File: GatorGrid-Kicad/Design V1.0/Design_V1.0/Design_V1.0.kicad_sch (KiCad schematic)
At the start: 10 parts, among them J1 Conn_01x02, U1 TP4056

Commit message: added all the symbols
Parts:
- added C1, C2: 100nF, symbol Device:C
- added F1: Polyfuse, symbol Device:Polyfuse
- added SW1: SW_SPST, symbol Switch:SW_SPST
- A1: value RaspberryPi_Pico -> RPICO-AP
- A2: value RaspberryPi_Pico -> RPICO-STA
- J1: value Conn_01x02 -> Battery-Connector
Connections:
- net GND: now also C1.2, C2.2
- net VBAT(+): now also SW1.2 (B); no longer D1.2 (A)
- net VSYS: now also C1.1, C2.1
- new net: F1.2, SW1.1 (A)
- new net: D1.2 (A), F1.1
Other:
- moved on the sheet: A1, A2, D1, D2, D3, J1, R1, R2, R3, U1

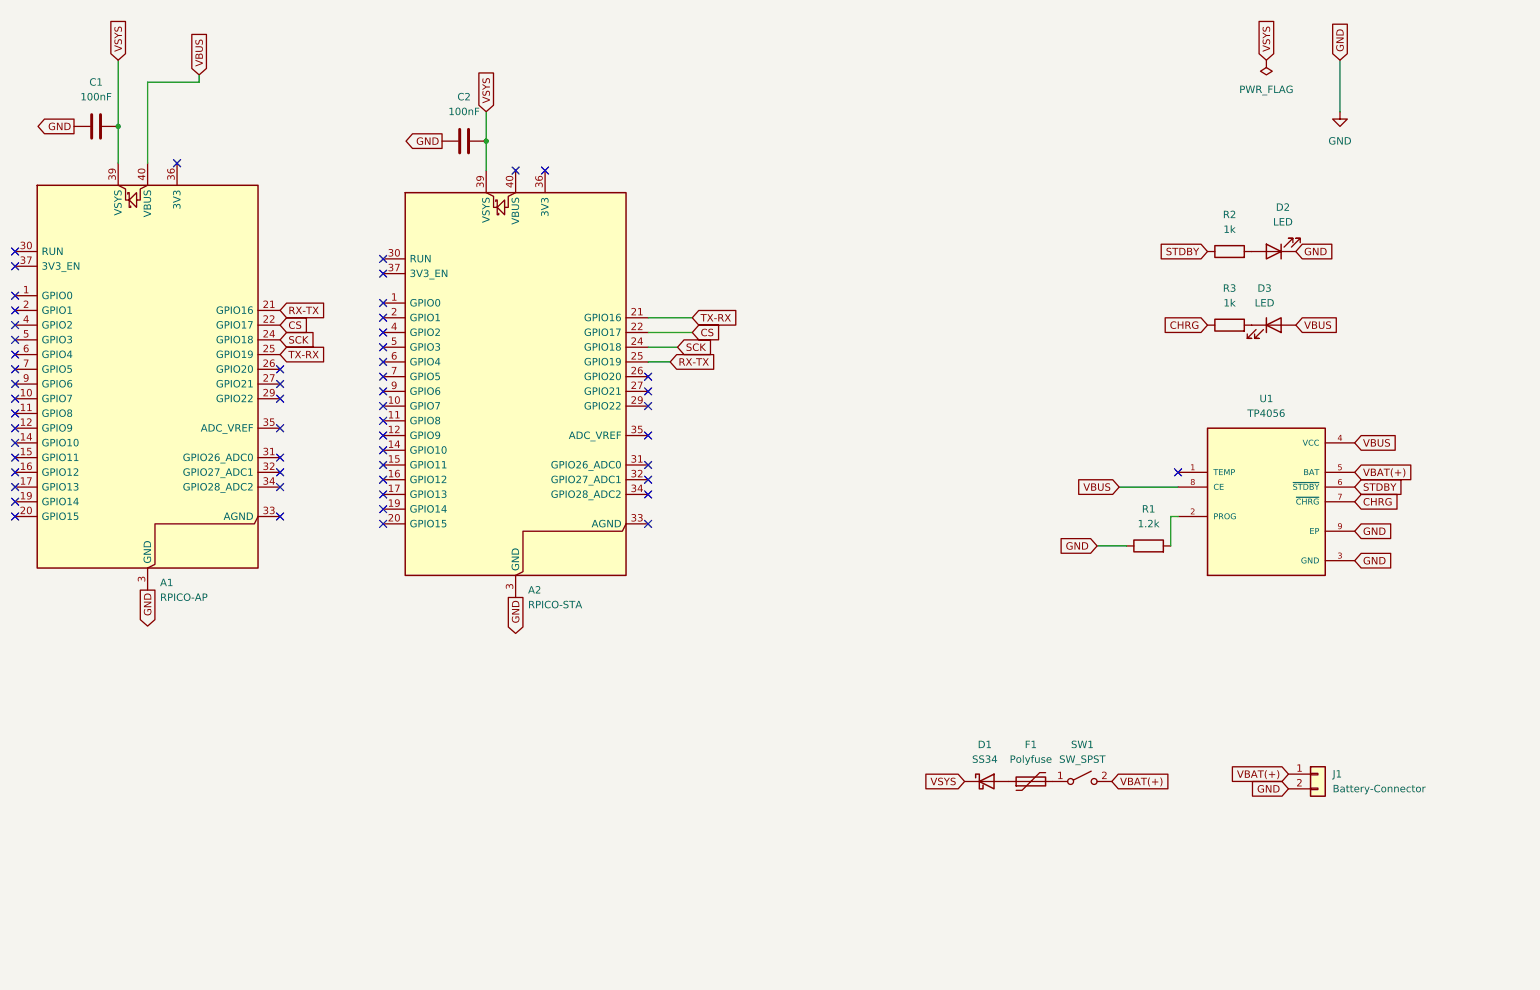
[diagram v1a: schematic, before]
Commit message: updated the schematic to have no errors on the error check
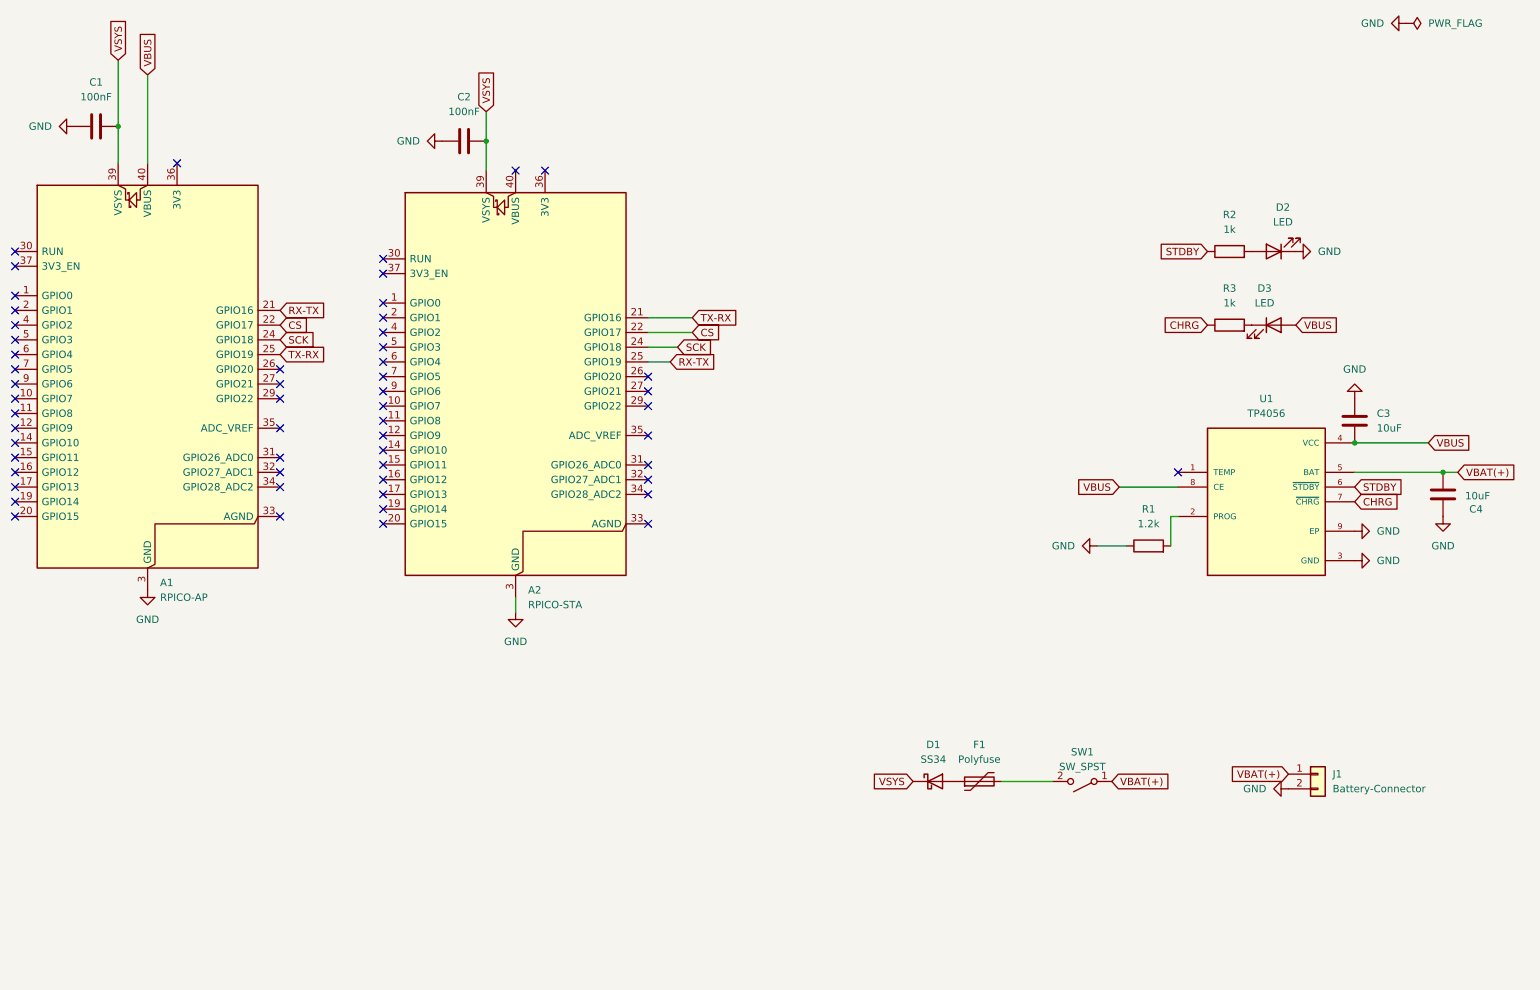
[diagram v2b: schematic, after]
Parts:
- added C3, C4: 10uF, symbol Device:C
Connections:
- net GND: now also C3.1, C4.1
- net VBAT(+): now also SW1.1 (A), C4.2; no longer SW1.2 (B)
- net VBUS: now also C3.2
- net at F1.2: now also SW1.2 (B); no longer SW1.1 (A)
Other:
- moved on the sheet: D1, F1, SW1

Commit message: updated PCB
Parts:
- C1, C2: footprint (none) -> Capacitor_THT:C_Disc_D5.0mm_W2.5mm_P2.50mm
- C3, C4: footprint (none) -> Capacitor_THT:C_Radial_D5.0mm_H11.0mm_P2.00mm
- D1: footprint Diode_SMD:D_SMA -> Diode_THT:D_DO-41_SOD81_P7.62mm_Horizontal
- F1: footprint (none) -> Fuse:Fuse_BelFuse_0ZRE0005FF_L8.3mm_W3.8mm
- SW1: footprint (none) -> Button_Switch_THT:SW_Slide_SPDT_Angled_CK_OS102011MA1Q
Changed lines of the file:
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@@
 			)
 		)
-		(property "Footprint" ""
+		(property "Footprint" "Button_Switch_THT:SW_Slide_SPDT_Angled_CK_OS102011MA1Q"
 			(at 207.01 152.4 0)
 			(effects
@@
 			)
 		)
-		(property "Footprint" ""
+		(property "Footprint" "Capacitor_THT:C_Radial_D5.0mm_H11.0mm_P2.00mm"
 			(at 268.2748 99.06 0)
 			(effects
@@
 			)
 		)
-		(property "Footprint" ""
+		(property "Footprint" "Capacitor_THT:C_Radial_D5.0mm_H11.0mm_P2.00mm"
 			(at 254.9652 93.98 0)
 			(effects
@@
 			)
 		)
-		(property "Footprint" ""
+		(property "Footprint" "Capacitor_THT:C_Disc_D5.0mm_W2.5mm_P2.50mm"
 			(at 96.52 42.8752 0)
 			(effects
@@
 			)
 		)
-		(property "Footprint" ""
+		(property "Footprint" "Fuse:Fuse_BelFuse_0ZRE0005FF_L8.3mm_W3.8mm"
 			(at 194.31 151.13 0)
 			(effects
@@
 			)
 		)
-		(property "Footprint" "Diode_SMD:D_SMA"
+		(property "Footprint" "Diode_THT:D_DO-41_SOD81_P7.62mm_Horizontal"
 			(at 181.61 156.845 0)
 			(effects
@@
 			)
 		)
-		(property "Footprint" ""
+		(property "Footprint" "Capacitor_THT:C_Disc_D5.0mm_W2.5mm_P2.50mm"
 			(at 33.02 40.3352 0)
 			(effects
